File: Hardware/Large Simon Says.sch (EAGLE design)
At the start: 25 parts, among them Q1 2N3904, Q2 2N3904, Q3 2N3904, Q4 2N3904, U1 ARDUINO_SHIELD, U2 AUDIO-AMP

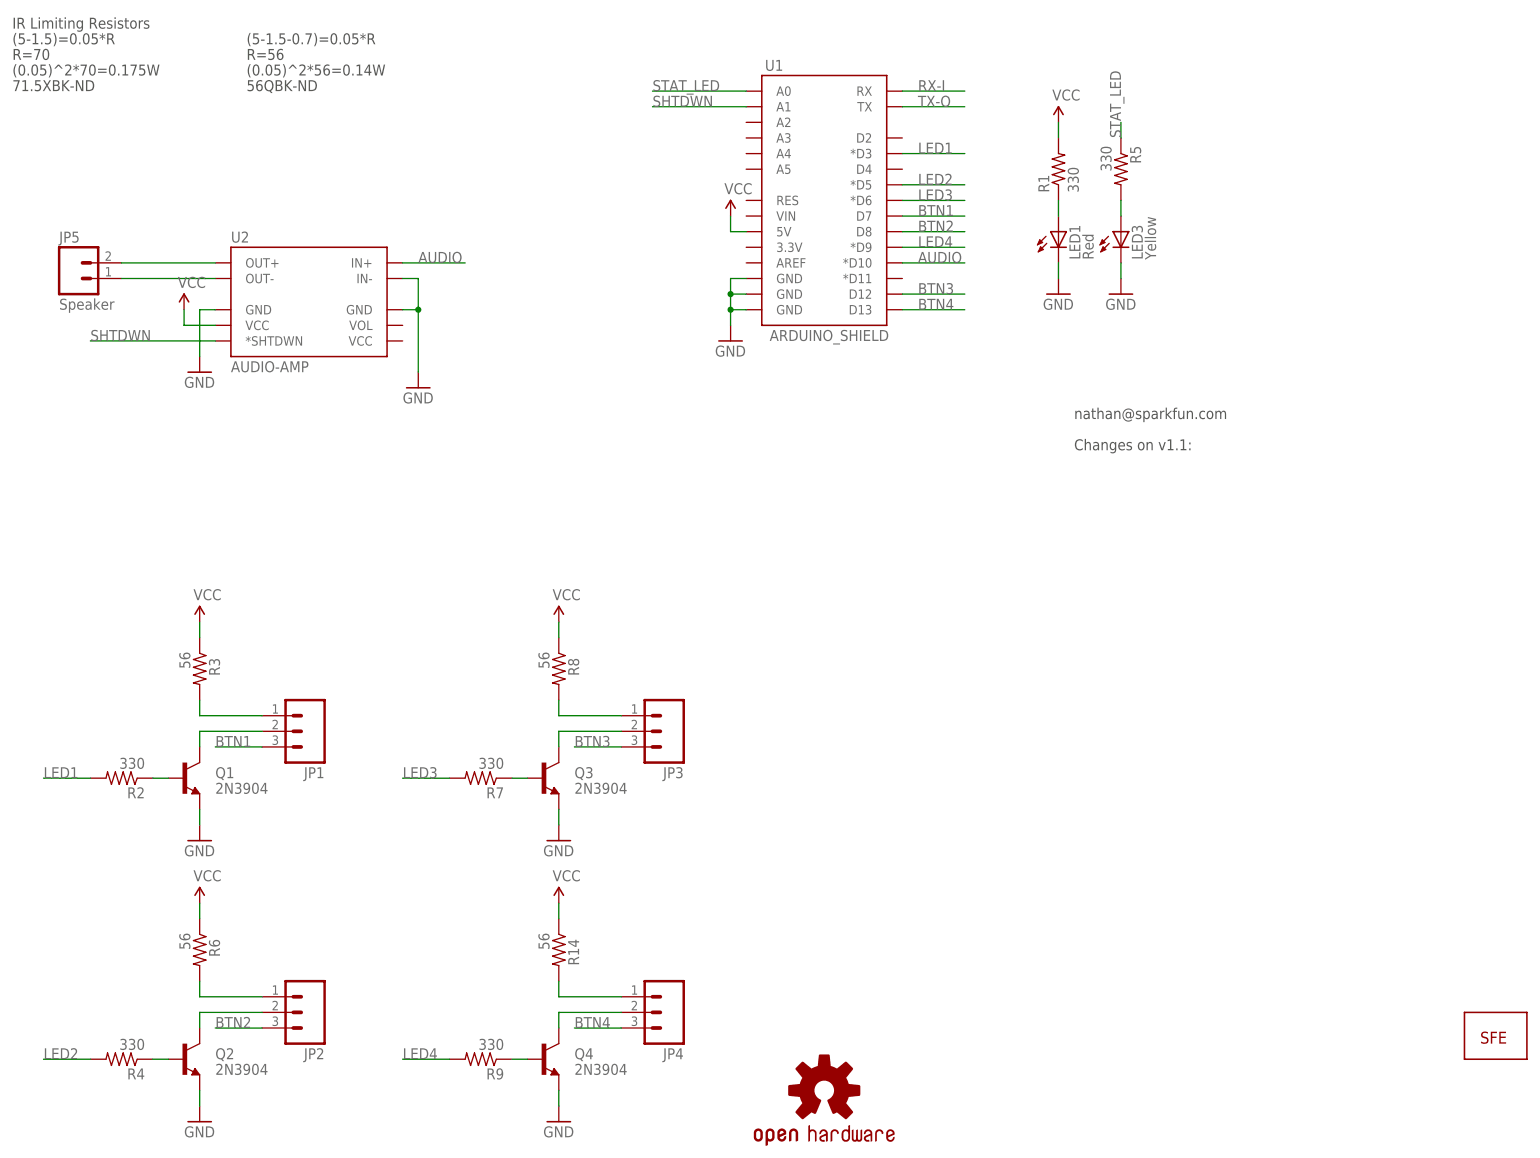
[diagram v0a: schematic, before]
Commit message: Adding firmware. Small changes to hardware.
The button connectors are missing a ground connection. Thought I could
do it with three, but it was a mistake.
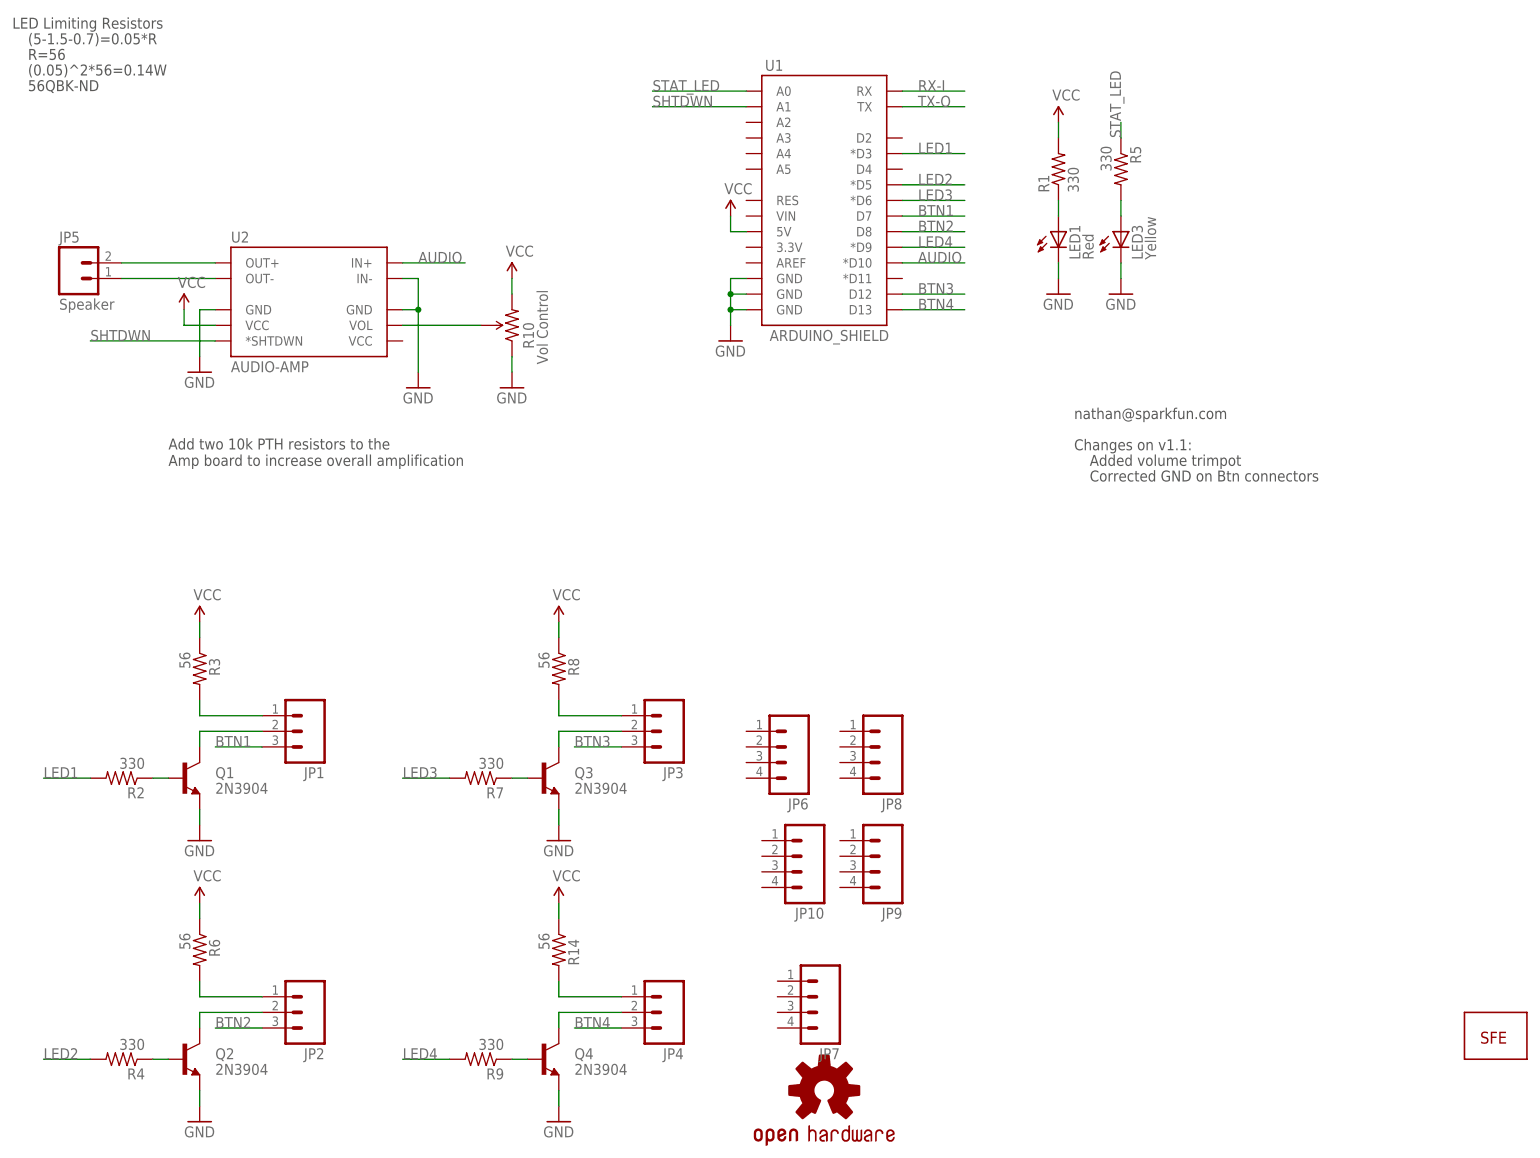
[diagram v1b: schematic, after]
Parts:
- added JP10, JP6, JP7, JP8, JP9: (no value), SparkFun-Connectors:M04JST-PTH
- added R10: Vol Control, SparkFun-Electromechanical:TRIMPOT-PTH-KNOB
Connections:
- new net N$14: R10.WIPER, U2.VOL
- net GND: now also R10.CCW
- net VCC: now also R10.CW
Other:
- note added: "Add two 10k PTH resistors to the Amp board to increase overall amplification"
- note added: "Added volume trimpot"
- note added: "Corrected GND on Btn connectors"
- note added: "LED Limiting Resistors"
- note removed: "(0.05)^2*70=0.175W"
- note removed: "(5-1.5)=0.05*R"
- note removed: "71.5XBK-ND"
- note removed: "IR Limiting Resistors"
- note removed: "R=70"
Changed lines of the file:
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@@
 <part name="GND7" library="SparkFun" deviceset="GND" device=""/>
 <part name="JP5" library="SparkFun-Connectors" deviceset="M02" device="JST-PTH-2" value="Speaker"/>
+<part name="R10" library="SparkFun-Electromechanical" deviceset="TRIMPOT" device="-PTH-KNOB" value="Vol Control"/>
+<part name="P+7" library="SparkFun" deviceset="VCC" device=""/>
+<part name="GND8" library="SparkFun" deviceset="GND" device=""/>
+<part name="JP6" library="SparkFun-Connectors" deviceset="M04" device="JST-PTH"/>
+<part name="JP7" library="SparkFun-Connectors" deviceset="M04" device="JST-PTH"/>
+<part name="JP8" library="SparkFun-Connectors" deviceset="M04" device="JST-PTH"/>
+<part name="JP9" library="SparkFun-Connectors" deviceset="M04" device="JST-PTH"/>
+<part name="JP10" library="SparkFun-Connectors" deviceset="M04" device="JST-PTH"/>
 </parts>
 <sheets>
@@
 <text x="175.26" y="114.3" size="1.778" layer="97">Changes on v1.1:</text>
 <text x="175.26" y="119.38" size="1.778" layer="97">nathan@sparkfun.com</text>
-<text x="2.54" y="180.34" size="1.778" layer="97">(5-1.5)=0.05*R</text>
-<text x="2.54" y="177.8" size="1.778" layer="97">R=70</text>
-<text x="2.54" y="175.26" size="1.778" layer="97">(0.05)^2*70=0.175W</text>
-<text x="2.54" y="172.72" size="1.778" layer="97">71.5XBK-ND</text>
-<text x="2.54" y="182.88" size="1.778" layer="97">IR Limiting Resistors</text>
-<text x="40.64" y="180.34" size="1.778" layer="97">(5-1.5-0.7)=0.05*R</text>
-<text x="40.64" y="177.8" size="1.778" layer="97">R=56</text>
-<text x="40.64" y="175.26" size="1.778" layer="97">(0.05)^2*56=0.14W</text>
-<text x="40.64" y="172.72" size="1.778" layer="97">56QBK-ND</text>
+<text x="2.54" y="182.88" size="1.778" layer="97">LED Limiting Resistors</text>
+<text x="5.08" y="180.34" size="1.778" layer="97">(5-1.5-0.7)=0.05*R</text>
+<text x="5.08" y="177.8" size="1.778" layer="97">R=56</text>
+<text x="5.08" y="175.26" size="1.778" layer="97">(0.05)^2*56=0.14W</text>
+<text x="5.08" y="172.72" size="1.778" layer="97">56QBK-ND</text>
+<text x="27.94" y="111.76" size="1.778" layer="97">Add two 10k PTH resistors to the
+Amp board to increase overall amplification</text>
+<text x="177.8" y="111.76" size="1.778" layer="97">Added volume trimpot</text>
+<text x="177.8" y="109.22" size="1.778" layer="97">Corrected GND on Btn connectors</text>
 </plain>
 <instances>
@@
 <instance part="GND7" gate="1" x="68.58" y="124.46"/>
 <instance part="JP5" gate="G$1" x="12.7" y="142.24"/>
+<instance part="R10" gate="R?" x="83.82" y="134.62" smashed="yes" rot="R90">
+<attribute name="NAME" x="87.4014" y="130.81" size="1.778" layer="95" rot="R90"/>
+<attribute name="VALUE" x="89.662" y="128.27" size="1.778" layer="96" rot="R90"/>
+</instance>
+<instance part="P+7" gate="1" x="83.82" y="142.24"/>
+<instance part="GND8" gate="1" x="83.82" y="124.46"/>
+<instance part="JP6" gate="G$1" x="127" y="66.04" rot="R180"/>
+<instance part="JP7" gate="G$1" x="132.08" y="25.4" rot="R180"/>
+<instance part="JP8" gate="G$1" x="142.24" y="66.04" rot="R180"/>
+<instance part="JP9" gate="G$1" x="142.24" y="48.26" rot="R180"/>
+<instance part="JP10" gate="G$1" x="129.54" y="48.26" rot="R180"/>
 </instances>
 <busses>
@@
 <pinref part="GND7" gate="1" pin="GND"/>
 </segment>
+<segment>
+<pinref part="R10" gate="R?" pin="CCW"/>
+<pinref part="GND8" gate="1" pin="GND"/>
+<wire x1="83.82" y1="127" x2="83.82" y2="129.54" width="0.1524" layer="91"/>
+</segment>
 </net>
 <net name="N$1" class="0">
@@
 <pinref part="P+5" gate="1" pin="VCC"/>
 </segment>
+<segment>
+<pinref part="R10" gate="R?" pin="CW"/>
+<pinref part="P+7" gate="1" pin="VCC"/>
+<wire x1="83.82" y1="142.24" x2="83.82" y2="139.7" width="0.1524" layer="91"/>
+</segment>
 </net>
 <net name="N$4" class="0">
@@
 </segment>
 </net>
+<net name="N$14" class="0">
+<segment>
+<pinref part="U2" gate="U1" pin="VOL"/>
+<pinref part="R10" gate="R?" pin="WIPER"/>
+<wire x1="66.04" y1="134.62" x2="78.74" y2="134.62" width="0.1524" layer="91"/>
+</segment>
+</net>
